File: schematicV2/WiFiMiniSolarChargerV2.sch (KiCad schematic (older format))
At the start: 17 parts, among them J1 Solar panel 12-20V, J2 Battery 12V, Q1 IRF4905, Q2 IRF4905, Q3 2N3904, Q4 2N3904, U1 MP2307_DC-DCconvertermodule, U2 WeMosD1MiniPro

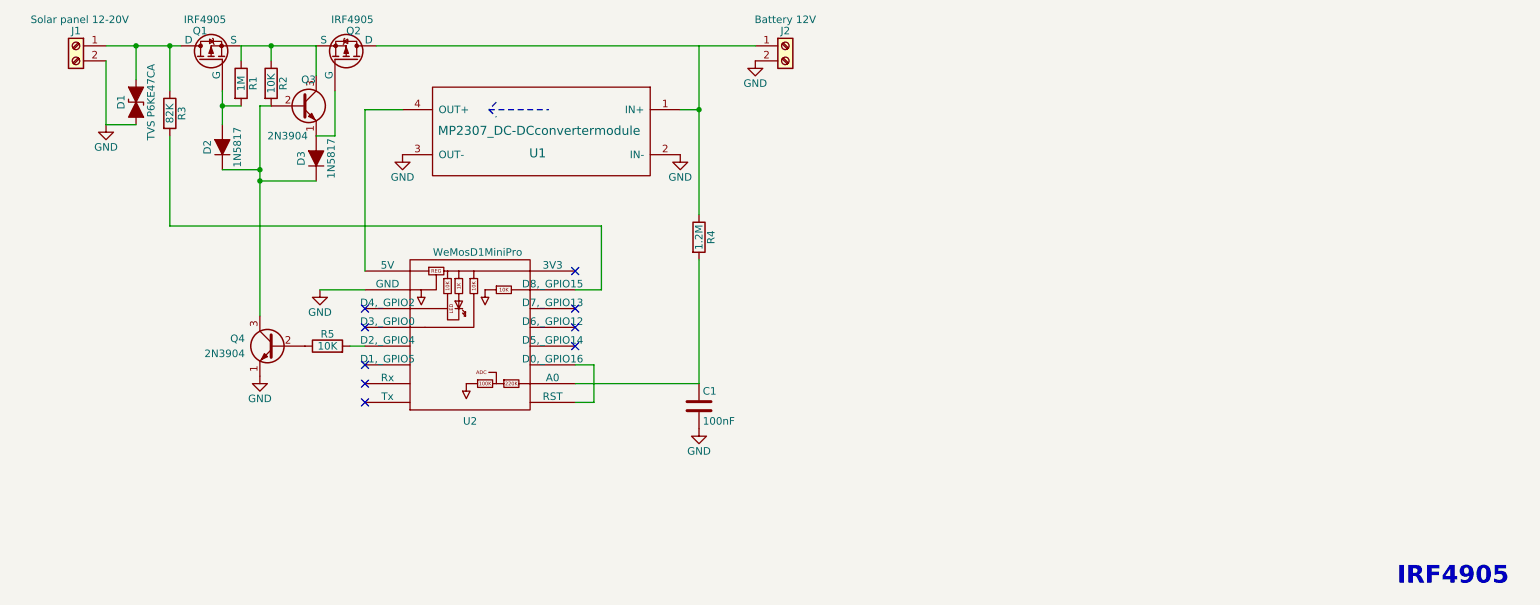
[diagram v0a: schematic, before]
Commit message: updates to support PWM
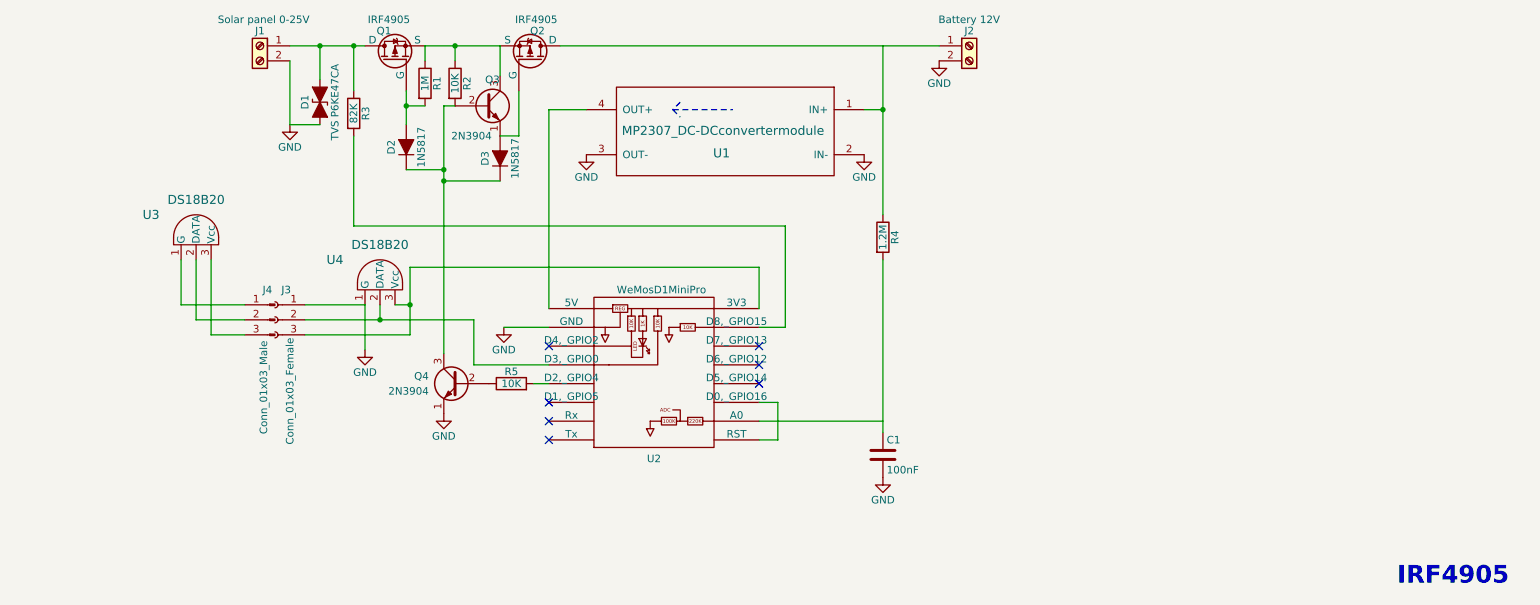
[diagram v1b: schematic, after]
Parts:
- added J3: Conn_01x03_Female, symbol Conn_01x03_Female
- added J4: Conn_01x03_Male, symbol Conn_01x03_Male
- added U3, U4: DS18B20, symbol DS18B20
- J1: value Solar panel 12-20V -> Solar panel 0-25V
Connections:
- wire segments 33 -> 59
- no-connect marks 9 -> 7
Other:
- moved on the sheet: C1, D1, D2, D3, J1, J2, Q1, Q2, Q3, Q4, R1, R2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
